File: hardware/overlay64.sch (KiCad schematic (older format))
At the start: 23 parts, among them IC1 ATMEGA328P-P, P1 ISP, P2 MAIN, P3 CONTROL, P4 BYPASS, P5 INPUT, P6 HOLE, P7 HOLE, P8 HOLE, P9 HOLE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

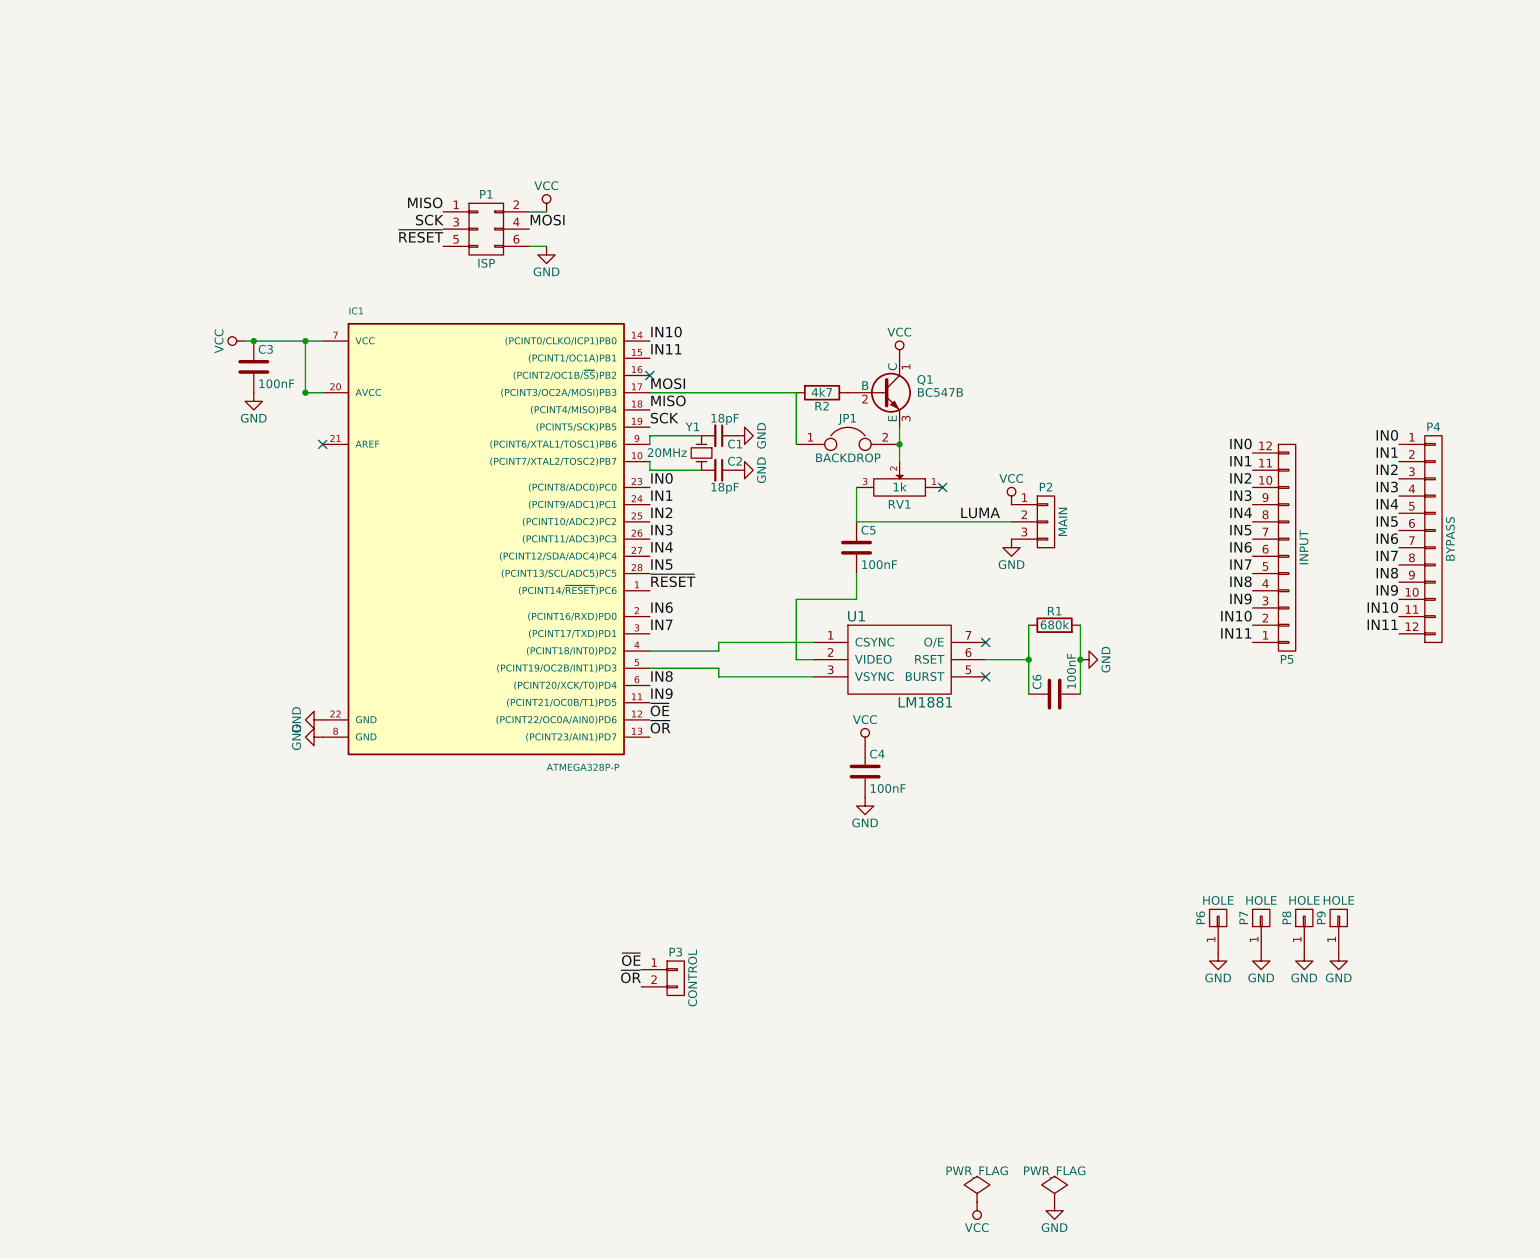
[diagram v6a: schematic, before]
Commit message: Hardware: Changed schematics for 1284p, removed pcb layout
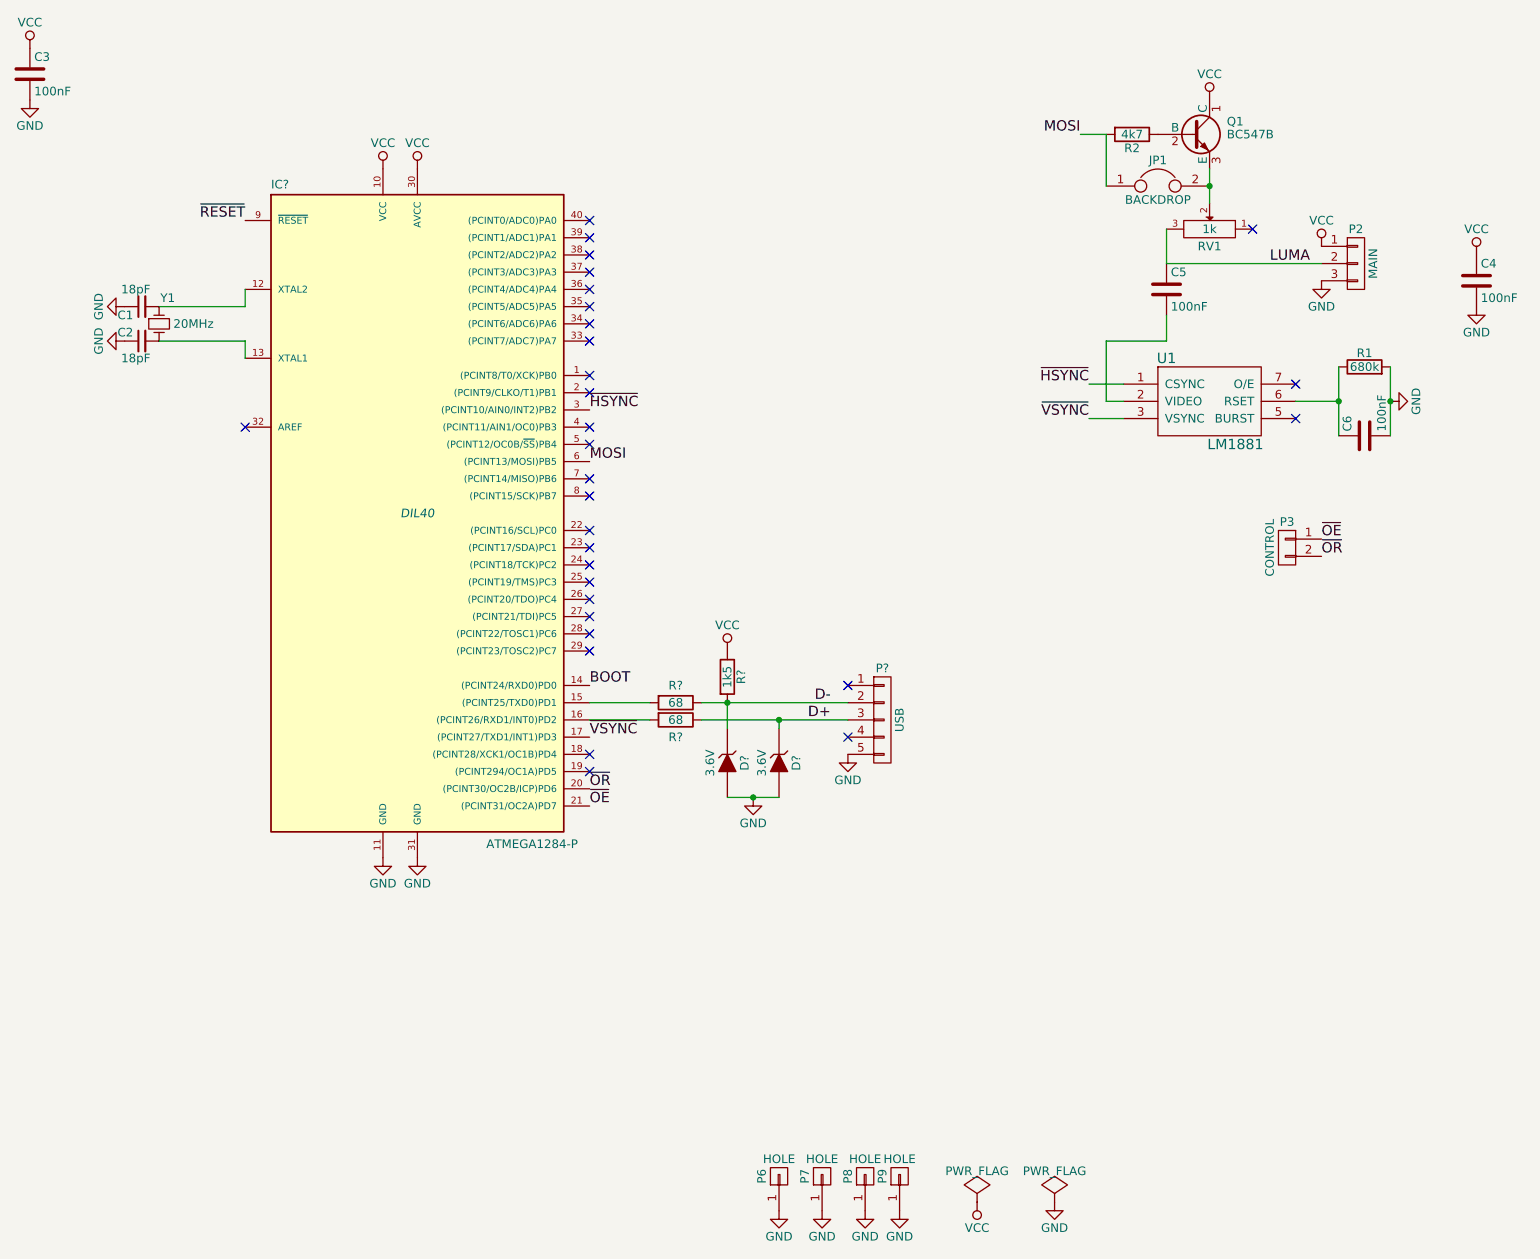
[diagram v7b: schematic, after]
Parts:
- removed IC1: ATMEGA328P-P, Housings_DIP:DIP-28_W7.62mm, symbol ATMEGA328P-P
- removed P1: ISP, Pin_Headers:Pin_Header_Straight_2x03, symbol CONN_02X03
- removed P4: BYPASS, Pin_Headers:Pin_Header_Angled_1x12, symbol CONN_01X12
- removed P5: INPUT, Pin_Headers:Pin_Header_Angled_1x12, symbol CONN_01X12
- added D? (x2): 3.6V, symbol ZENER
- added IC?: ATMEGA1284-P, DIL40, symbol ATMEGA1284-P
- added P?: USB, symbol CONN_01X05
- added R? (x2): 68, symbol R
- added R?: 1k5, symbol R
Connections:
- net GND: now also D?.2 (A), D?.2 (A), IC?.11 (GND), IC?.31 (GND), P?.5 (P5)
- net MOSI: now also IC?.6 ((PCINT13/MOSI)PB5)
- net VCC: now also IC?.10 (VCC), IC?.30 (AVCC), R?.1
- net ~OE: now also IC?.21 ((PCINT31/OC2A)PD7)
- net ~OR: now also IC?.20 ((PCINT30/OC2B/ICP)PD6)
- net ~RESET: now also IC?.9 (~RESET)
- net ~HSYNC: now reaches U1.1 (CSYNC)
- net ~HSYNC: now also IC?.3 ((PCINT10/AIN0/INT2)PB2)
- net ~VSYNC: now reaches U1.3 (VSYNC)
- net ~VSYNC: now also IC?.17 ((PCINT27/TXD1/INT1)PD3)
- net at C1.2, Y1.1: now also IC?.12 (XTAL2)
- net at C2.2, Y1.2: now also IC?.13 (XTAL1)
- new net: IC?.15 ((PCINT25/TXD0)PD1), R?.2
- new net: IC?.16 ((PCINT26/RXD1/INT0)PD2), R?.2
- new net BOOT: IC?.14 ((PCINT24/RXD0)PD0)
- new net D+: D?.1 (K), P?.3 (P3), R?.1
- new net D-: D?.1 (K), P?.2 (P2), R?.1, R?.2
- no-connect marks 5 -> 30
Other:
- moved on the sheet: C1, C2, C3, C4, C5, C6, JP1, P2, P3, P6, P7, P8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
